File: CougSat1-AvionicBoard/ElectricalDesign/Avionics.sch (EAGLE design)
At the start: 117 parts, among them J3 SWD, J4 CougSat Card, J7 CougSat Card, J8 SWD, J9 SWD, U1 STM32L476RGT, U10 BNO055, U11 128KB, U12 TXS0102DQM, U13 TXS0102DQM, U14 LTC2499, U2 STM32L476RGT, U3 STM32L476RGT, U4 128KB, U5 DRV8837, U6 DRV8837, U7 DRV8837, U8 LTC2499, U9 Venus838FLPx-L, Y1 16MHz ±10ppm, Y2 32.768kHz ±10ppm, Y3 16MHz ±10ppm, Y4 32.768kHz ±10ppm, Y5 16MHz ±10ppm, Y6 32.768kHz ±10ppm, Y7 32.768kHz ±10ppm

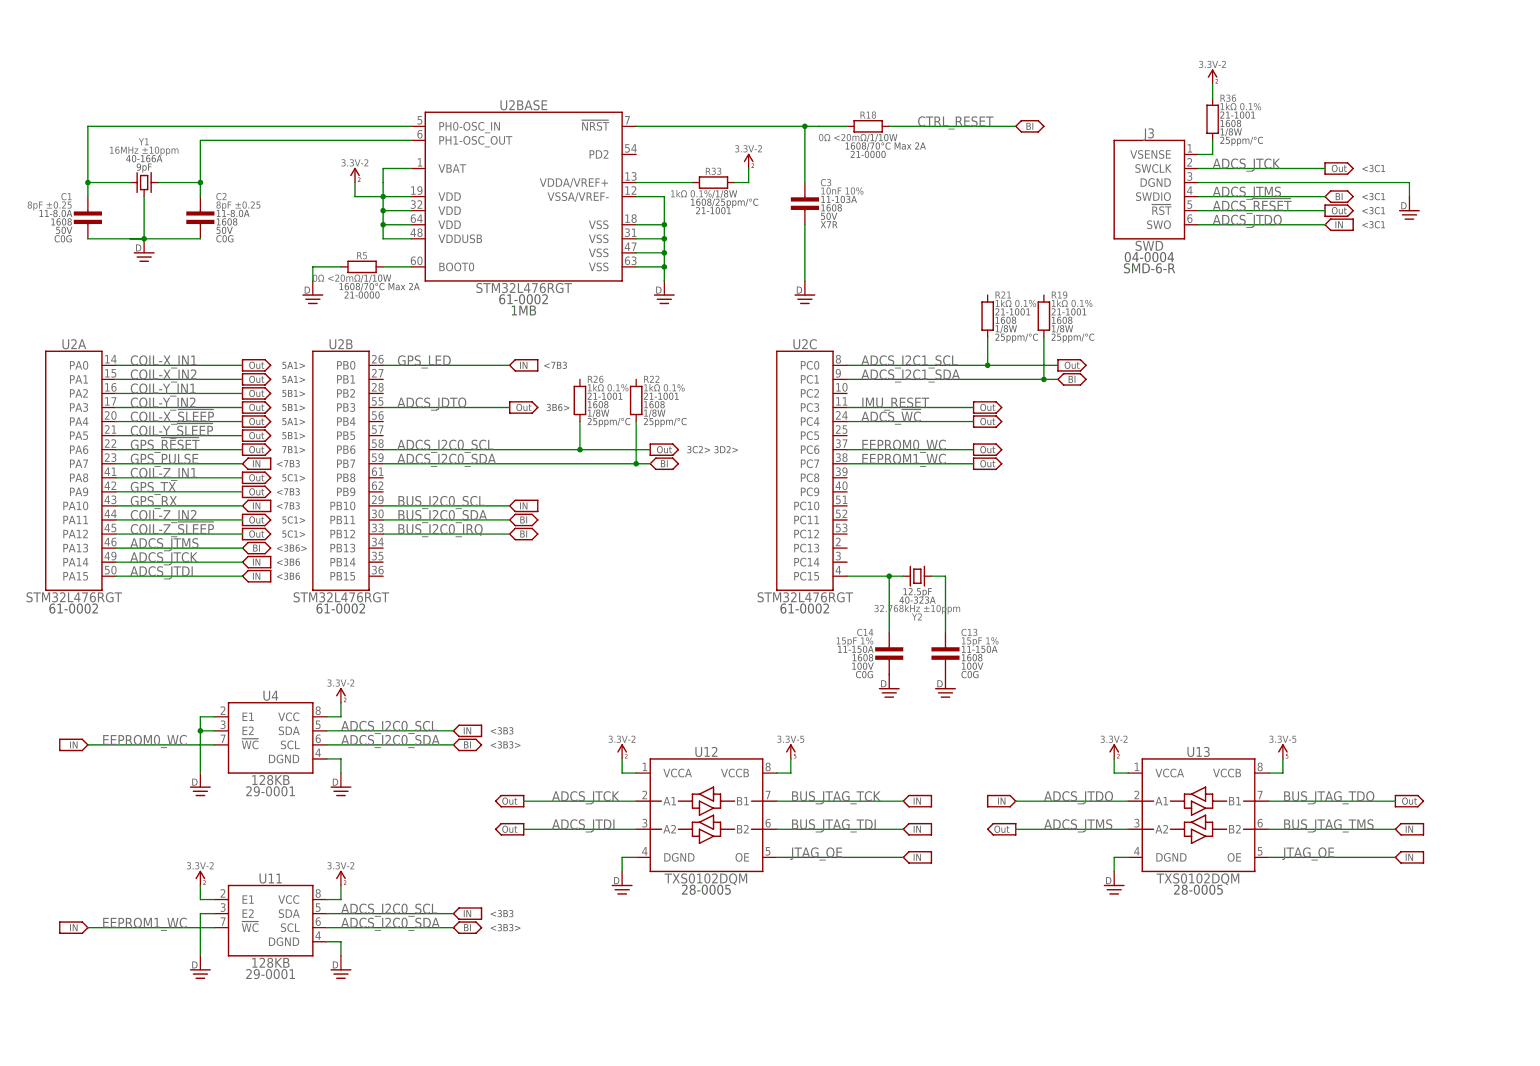
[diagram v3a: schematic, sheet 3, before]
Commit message: Added Final Components to Schematic
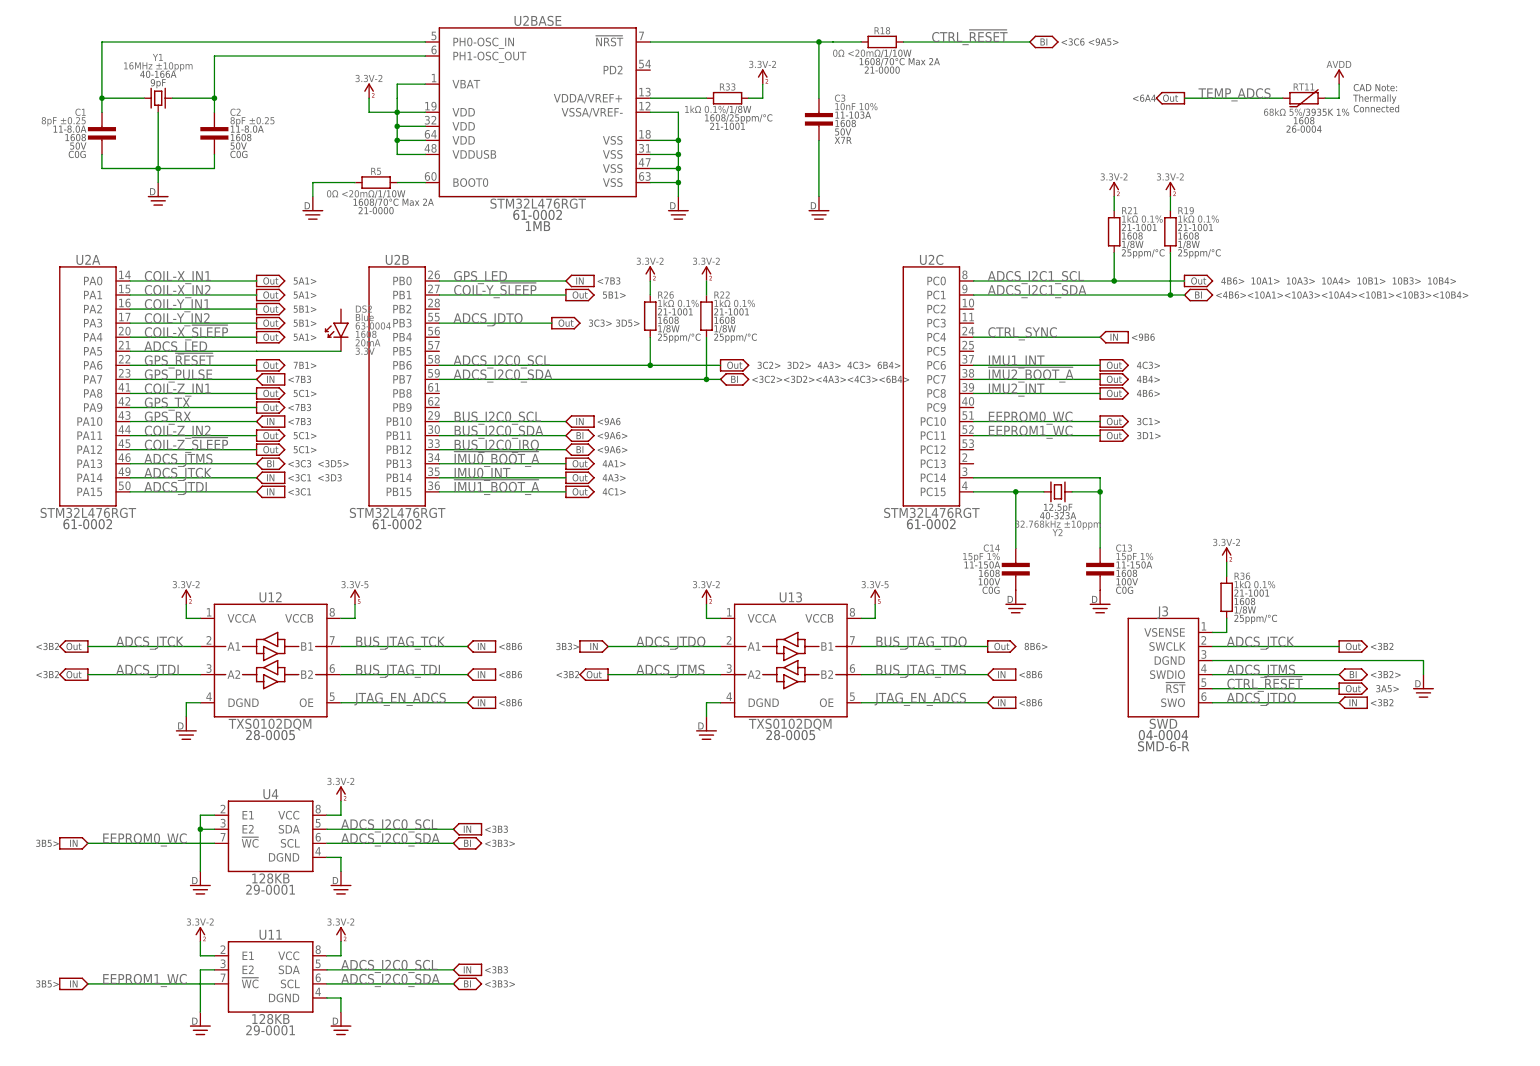
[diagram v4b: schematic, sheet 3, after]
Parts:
- removed L1, L2, L3: xxx Turns, CougsInSpace-Coils:MAGNETORQUER-1UPV-SMD-3030
- added C32, C38: 10nF 10%, CougsInSpace-Capacitors:CAP-H-10NF-1608
- added C33, C39: 100nF 10%, CougsInSpace-Capacitors:CAP-V-100NF-3216
- added C34, C40: 6.8nF 5%, CougsInSpace-Capacitors:CAP-V-6.8NF-1608
- added C35, C41: 100nF 10%, CougsInSpace-Capacitors:CAP-V-100NF-1608
- added C36, C37, C42, C43: 15pF 1%, CougsInSpace-Capacitors:CAP-V-15PF-1608
- added DS2: Blue, CougsInSpace-LEDs:LED-V-BLU-1608
- added R32, R39, R40, R41: 10kΩ 0.1%, CougsInSpace-Resistors:RES-V-10K-1608
- added RT10, RT11, RT12, RT13, RT14, RT8, RT9: 68kΩ 5%, CougsInSpace-Resistors:THERMISTOR-H-68K-1608
- added U15, U16: BNO055, CougsInSpace-Sensors:BNO055
- added Y8, Y9: 32.768kHz ±10ppm, CougsInSpace-Clocks:CRYSTAL-32.768KHZ-SMD3.2X1.5
- J11: value (none) -> -Y
- J12: value (none) -> +Z
- J13: value (none) -> +X
- J14: value (none) -> -Z
- J15: value (none) -> +Y
- J5: value (none) -> -X
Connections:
- net JTAG_OE renamed JTAG_EN_ADCS
- net SPI3_MISO renamed IHU_SPI2_MISO
- net SYS_JTDI renamed IHU_JTDI
- removed net !IMU0_BOOT-A: R25.2, U10.!BOOT_LOAD_PIN
- removed net ADCS_!RESET: J3.!RST
- removed net ADCS_!WC: U2C.PC4
- removed net CTRL_RESET: R18.2, R24.2, R28.2
- removed net I2C_SCL: J11.3, J12.3, J13.3, J14.3, J15.3, J5.3
- removed net I2C_SDA: J11.2, J12.2, J13.2, J14.2, J15.2, J5.2
- removed net IFJR_!RESET: J8.!RST
- removed net IHU_!RESET: J9.!RST
- removed net IMU_RESET: U2C.PC3
- removed net N$11: L2.2, U6.OUT2
- removed net N$14: L3.2, U7.OUT2
- removed net N$31: C20.2, C21.2
- removed net N$33: J16.CD/DAT3
- removed net N$39: C4.1
- removed net N$40: J6.CD/DAT3
- removed net N$41: J2.CMD, J6.CMD
- removed net N$42: U1BASE.VBAT, U1BASE.VDD@1, U1BASE.VDD@2, U1BASE.VDD@3, U1BASE.VDDUSB
- removed net N$43: J2.CLK, J6.CLK
- removed net N$45: J2.DAT0, J6.DAT0
- removed net N$46: J6.SW+
- removed net N$47: J2.CD/DAT3
- removed net N$5: C1.2, C2.2
- removed net N$50: J2.SW+
- removed net N$52: J7POWER.PR_3.3V-3
- removed net N$53: J7POWER.PR_3.3V-4
- removed net N$54: J7POWER.PR_3.3V-5
- removed net N$55: J10.CMD, J16.CMD
- removed net N$56: J10.CLK, J16.CLK
- removed net N$57: J10.DAT0, J16.DAT0
- removed net N$70: J16.SW+
- removed net N$71: J10.CD/DAT3
- removed net N$72: J10.SW+
- removed net N$9: L1.2, U5.OUT2
- removed net SPI1_MISO: J4DATA.BUS_SPI_MISO, U1A.PA6, U3A.PA6
- removed net SPI1_MOSI: J4DATA.BUS_SPI_MOSI, U1A.PA7, U3A.PA7
- removed net SPI1_SCK: J4DATA.BUS_SPI_SCK, U1A.PA5, U3A.PA5
- removed net SPI2_MISO: U3C.PC2
- removed net SPI2_MOSI: U3C.PC3
- removed net SPI2_SCK: U3B.PB10
- removed net SPI3_MOSI: U3C.PC12
- removed net SPI3_SCK: U3C.PC10
- removed net SYS_JTCK-SWCLK: U3A.PA14
- removed net SYS_JTDO-SWO: U3B.PB3
- removed net SYS_JTMS-SWDIO: U3A.PA13
- removed net TEMP_IMU: U8.CH7
- new net !IMU0_BOOT_A: R25.2, U10.!BOOT_LOAD_PIN, U2B.PB13
- new net !IMU1_BOOT_A: R39.2, U15.!BOOT_LOAD_PIN, U2B.PB15
- new net !IMU2_BOOT_A: R41.2, U16.!BOOT_LOAD_PIN, U2C.PC7
- new net ADCS_LED: DS2.C, U2A.PA5
- new net COIL-X_COIL-: J5.4, U5.OUT2
- new net COIL-Y_COIL-: J11.4, U6.OUT2
- new net COIL-Z_+: J12.3
- new net COIL-Z_COIL-: J12.4, U7.OUT2
- new net IFJR_SD_CS0: J16.CD/DAT3, U1A.PA8
- new net IFJR_SD_CS1: J10.CD/DAT3, U1A.PA10
- new net IFJR_SD_SW0: J16.SW+, U1A.PA9
- new net IFJR_SD_SW1: J10.SW+, U1A.PA11
- new net IFJR_SPI0_MISO: J10.DAT0, J16.DAT0, U1A.PA6
- new net IFJR_SPI0_MOSI: J10.CMD, J16.CMD, U1A.PA7
- new net IFJR_SPI0_SCK: J10.CLK, J16.CLK, U1A.PA5
- new net IHU_SD_CS0: J6.CD/DAT3, U3C.PC5
- new net IHU_SD_CS1: J2.CD/DAT3, U3B.PB1
- new net IHU_SD_SW0: J6.SW+, U3B.PB0
- new net IHU_SD_SW1: J2.SW+, U3B.PB2
- new net IHU_SPI0_MISO: J4DATA.BUS_SPI_MISO, U3A.PA6
- new net IHU_SPI0_MOSI: J4DATA.BUS_SPI_MOSI, U3A.PA7
- new net IHU_SPI0_SCK: J4DATA.BUS_SPI_SCK, U3A.PA5
- new net IHU_SPI1_MISO: J4DATA.COM_SPI_MISO, U3C.PC2
- new net IHU_SPI1_MOSI: J4DATA.COM_SPI_MOSI, U3C.PC3
- new net IHU_SPI1_SCK: J4DATA.COM_SPI_SCK, U3B.PB10
- new net IHU_SPI2_MOSI: J2.CMD, J2.DAT0, J6.CMD, J6.DAT0, U3C.PC12
- new net IHU_SPI2_SCK: J2.CLK, J6.CLK, U3C.PC10
- new net IMU1_INT: U15.INT, U2C.PC6
- new net IMU2_INT: U16.INT, U2C.PC8
- new net N$20: C32.2, U15.CAP
- new net N$49: C36.1, U15.XOUT32, Y8.1
- new net N$63: C37.1, U15.XIN32, Y8.2
- new net N$66: C38.2, U16.CAP
- new net N$68: C42.1, U16.XOUT32, Y9.1
- new net N$69: C43.1, U16.XIN32, Y9.2
- new net TEMP_IMU0: RT8.1, U8.CH7
- new net TEMP_IMU1: RT9.1, U8.CH9
- new net TEMP_IMU2: RT10.1, U8.CH10
- net !IMU_RESET: now also R32.1, R40.1, U15.!RESET, U15.COM3, U16.!RESET
- net 3.3V: no longer J11.1, J12.1, J13.1, J14.1, J15.1, J5.1
- net 3.3V_2: now also J13.3, J14.3, R19.2, R21.2, R22.2, R26.2
- net 3.3V_3: now also C33.2, C34.2, C35.2, C39.2, C40.2, C41.2, J7POWER.PR_3.3V-3, R32.2, R39.1, R40.2, R41.1, U15.VDD, U15.VDDIO, U16.VDD, U16.VDDIO
- net 3.3V_4: now also J7POWER.PR_3.3V-4
- net 3.3V_5: now also J7POWER.PR_3.3V-5, U1BASE.VBAT, U1BASE.VDD@1, U1BASE.VDD@2, U1BASE.VDD@3, U1BASE.VDDUSB
- net ADCS_I2C0_SCL: now also U15.COM1
- net ADCS_I2C0_SDA: now also U15.COM0
- net ADCS_I2C1_SCL: now also J11.1, J12.1, J13.1, J14.1, J15.1, J5.1, U16.COM1
- net ADCS_I2C1_SDA: now also J11.2, J12.2, J13.2, J14.2, J15.2, J5.2, U16.COM0
- net AVDD: now also RT10.2, RT11.2, RT12.2, RT13.2, RT14.2, RT8.2, RT9.2
- net COIL-X_COIL+: now also J5.3; no longer L1.1
- net COIL-Y_!SLEEP: now also U2B.PB1; no longer U2A.PA5
- net COIL-Y_COIL+: now also J11.3; no longer L2.1
- net COIL-Z_COIL+: no longer L3.1
- net CTRL_!RESET: now also J3.!RST, J8.!RST, J9.!RST, R18.2, R24.2, R28.2, U3C.PC7
- net CTRL_SYNC: now also U1B.PB0, U2C.PC4, U3C.PC8
- net DGND: now also C1.2, C2.2, C20.2, C21.2, C32.1, C33.1, C34.1, C35.1, C36.2, C37.2, C38.1, C39.1, C4.1, C40.1, C41.1, C42.2, C43.2, U15.COM2, U15.DGND, U15.DGNDIO, U15.PS0, U15.PS1, U16.COM2, U16.COM3, U16.DGND, U16.DGNDIO, U16.PS0, U16.PS1; no longer J11.4, J12.4, J15.4, J5.4
- net EEPROM0_WC: now also U2C.PC10; no longer U2C.PC6
- net EEPROM1_WC: now also U2C.PC11; no longer U2C.PC7
- net IHU_JTCK: now also U3A.PA14
- net IHU_JTDO: now also U3B.PB3
- net IHU_JTMS: now also U3A.PA13
- net IMU0_INT: now also U2B.PB14
- net N$22: now also U2C.PC14
- net TEMP_ADCS: now also RT11.1, U8.CH11; no longer U8.CH9
- net TEMP_H-BRIDGE-X: now also U8.CH13; no longer U8.CH10
- net TEMP_H-BRIDGE-Y: now also U8.CH14; no longer U8.CH11
- net TEMP_H-BRIDGE-Z: now also U8.CH15; no longer U8.CH12
- net TEMP_IHU: now also RT14.1
- net TEMP_SD_IHU0: now also RT12.1
- net TEMP_SD_IHU1: now also RT13.1
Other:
- note added: "10A1>"
- note added: "10A3>"
- note added: "10A4>"
- note added: "3A5>"
- note added: "3B5>"
- note added: "3C1>"
- note added: "3C2> 3D2> 4A3> 4C3> 6B4>"
- note added: "3C3> 3D5>"
- note added: "3D1>"
- note added: "4A1>"
- note added: "4A3>"
- note added: "4B4>"
- note added: "4B6>"
- note added: "4B6> 10A1> 10A3> 10A4> 10B1> 10B3> 10B4>"
- note added: "4C1>"
- note added: "4C3>"
- note added: "5A2>"
- note added: "5A3>"
- note added: "5B2>"
- note added: "5B3>"
- note added: "5C2>"
- note added: "5C3>"
- note added: "6A1>"
- note added: "7C3>"
- note added: "8A2>"
- note added: "8A5>"
- note added: "8B2>"
- note added: "8B6>"
- note added: "8C2>"
- note added: "8C3>"
- note added: "8C6>"
- note added: "8D2>"
- note added: "8D3>"
- note added: "9A1>"
- note added: "9B2>"
- note added: "9B3>"
- note added: "9B4>"
- note added: "9B5>"
- note added: "9B6>"
- note added: "9C2>"
- note added: "9C4>"
- note added: "9D2>"
- note added: "9D4>"
- note added: "9D6>"
- note added: "<10A1"
- note added: "<10A3"
- note added: "<10A4"
- note added: "<3A5"
- note added: "<3B2>"
- note added: "<3B5"
- note added: "<3B5>"
- note added: "<3C1 <3D3"
- note added: "<3C2><3D2><4A3><4C3><6B4>"
- note added: "<3C3 <3D5>"
- note added: "<3C6 <9A5>"
- note added: "<4A1"
- note added: "<4B6><10A1><10A3><10A4><10B1><10B3><10B4>"
- note added: "<5A3"
- note added: "<5A4"
- note added: "<5B3"
- note added: "<5B4"
- note added: "<5C3"
- note added: "<5C4"
- note added: "<6A2"
- note added: "<6A4"
- note added: "<6C2"
- note added: "<8B2"
- note added: "<8B2>"
- note added: "<8B3"
- note added: "<8B4"
- note added: "<8B6"
- note added: "<8B6>"
- note added: "<8C2"
- note added: "<8C2>"
- note added: "<8C6"
- note added: "<8C6 <9A5>"
- note added: "<8C6>"
- note added: "<8D2"
- note added: "<9A6"
- note added: "<9A6>"
- note added: "<9B2"
- note added: "<9B2>"
- note added: "<9B3"
- note added: "<9B3 <3B3"
- note added: "<9B3>"
- note added: "<9B3><3B3>"
- note added: "<9B4"
- note added: "<9B4 3B5> 8B3>"
- note added: "<9B4><3A5><8A5><9A5>"
- note added: "<9B6"
- note added: "<9B6>"
- note added: "<9C2"
- note added: "<9C6"
- note added: "<9C6>"
- note added: "<9D2"
- note added: "<9D6 <9B6>"
- note added: "<9D6>"
- note added: "\ <3B3"
- note removed: "3B6>"
- note removed: "3C2> 3D2>"
- moved on the sheet: C1, C11, C12, C13, C14, C17, C18, C2, C23, C25, C26, C3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

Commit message: Update Avionics.sch
Adjusted schematic
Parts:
- removed C20, C21: 8pF ±0.25, CougsInSpace-Capacitors:CAP-V-8PF-1608
- removed J7: CougSat Card, CougsInSpace-Boards:CIS_CARD-OPEN+X
- removed Y5: 16MHz ±10ppm, CougsInSpace-Clocks:CRYSTAL-16MHZ-SMD3.2X1.5
- added C44, C46, C47, C48, C49, C54, C55, C56, C57, C60, C61, C62, C63: 100nF 10%, CougsInSpace-Capacitors:CAP-V-100NF-1608
- added C45: 100nF 10%, CougsInSpace-Capacitors:CAP-V-100NF-3216
- added C58, C59: 8pF ±0.25, CougsInSpace-Capacitors:CAP-V-8PF-1608
- added DS3: Yellow, CougsInSpace-LEDs:LED-H-YLW-1608
- added DS5: Green, CougsInSpace-LEDs:LED-H-GRN-1608
- added R42, R46: 1kΩ 0.1%, CougsInSpace-Resistors:RES-H-1K-1608
- added R43, R44: 10kΩ 0.1%, CougsInSpace-Resistors:RES-V-10K-1608
- added R45: 0Ω <20mΩ, CougsInSpace-Resistors:RES-H-0-1608
- added U17, U18: TXS0102DQM, CougsInSpace-IC-Logic:LEVEL_SHIFTER-2BIT-XSON-8
- added Y10: 16MHz ±10ppm, CougsInSpace-Clocks:CRYSTAL-16MHZ-SMD-4025
- C34: value 6.8nF 5% -> 100nF 10%; device CougsInSpace-Capacitors:CAP-V-6.8NF-1608 -> CougsInSpace-Capacitors:CAP-V-100NF-1608
- C35, C41, C8: value 100nF 10% -> 6.8nF 5%; device CougsInSpace-Capacitors:CAP-V-100NF-1608 -> CougsInSpace-Capacitors:CAP-V-6.8NF-1608
- C40, C6: value 6.8nF 5% -> 100nF 10%; device CougsInSpace-Capacitors:CAP-V-6.8NF-1608 -> CougsInSpace-Capacitors:CAP-V-100NF-3216
- DS2: device CougsInSpace-LEDs:LED-V-BLU-1608 -> CougsInSpace-LEDs:LED-H-BLU-1608
- R13: value 560Ω 1% -> 1kΩ 0.1%; device CougsInSpace-Resistors:RES-H-560R-1608 -> CougsInSpace-Resistors:RES-H-1K-1608
- R27: value 0Ω <20mΩ -> 1kΩ 0.1%; device CougsInSpace-Resistors:RES-H-0-1608 -> CougsInSpace-Resistors:RES-H-1K-1608
- Y1, Y3: device CougsInSpace-Clocks:CRYSTAL-16MHZ-SMD3.2X1.5 -> CougsInSpace-Clocks:CRYSTAL-16MHZ-SMD-4025
- Y2, Y4, Y6, Y7, Y8, Y9: device CougsInSpace-Clocks:CRYSTAL-32.768KHZ-SMD3.2X1.5 -> CougsInSpace-Clocks:CRYSTAL-32.768KHZ-SMD-3215
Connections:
- removed net 3.3V: C29.1, C7.1, U14.VCC, U8.VCC
- removed net ADCS_LED: DS2.C, U2A.PA5
- removed net COIL-X_SLEEP: U5.!SLEEP
- removed net COIL-Y_SLEEP: U6.!SLEEP
- removed net COIL-Z_SLEEP: U7.!SLEEP
- removed net IHU_GPIO-6: J4GPIO.GPIO-6, U3A.PA9
- removed net IHU_GPIO-7: J4GPIO.GPIO-7, U3A.PA10
- removed net IHU_GPIO-8: J4GPIO.GPIO-8, U3A.PA11
- removed net IHU_GPIO-9: J4GPIO.GPIO-9, U3A.PA12
- removed net N$32: R27.2, U3BASE.BOOT0
- removed net N$34: C20.1, U3BASE.PH0-OSC_IN, Y5.1
- new net IFJR_LED: DS5.A, U1A.PA4
- new net IHU_LED: DS2.A, DS3.A, U2A.PA5, U3A.PA9
- new net JTAG_EN_IHU: J4JTAG.BUS_JTAG_EN-1, U17.OE, U18.OE, U1C.PC4
- new net N$14: C58.1, U3BASE.PH0-OSC_IN, Y10.1
- new net N$15: C59.1, U3BASE.PH1-OSC_OUT, Y10.2
- new net N$21: R45.2, U3BASE.BOOT0
- new net N$31: DS5.C, R46.1
- new net N$5: DS2.C, R42.1
- net !IMU0_BOOT_A: now also R43.1; no longer R25.2
- net !IMU1_BOOT_A: now also R39.1; no longer R39.2
- net 3.3V_0: now also C60.1, C61.1, C62.1, C63.1, J4POWER.PR_3.3V-0, U14.CA0, U14.VCC; no longer J7POWER.PR_3.3V-0
- net 3.3V_1: now also J4POWER.PR_3.3V-1; no longer J7POWER.PR_3.3V-1
- net 3.3V_2: now also C46.1, C47.1, C48.1, C49.1, J4POWER.PR_3.3V-2, U17.VCCA, U18.VCCA, U8.VCC; no longer J7POWER.PR_3.3V-2
- net 3.3V_3: now also C33.1, C35.1, C39.1, C40.1, C41.1, C45.1, C5.1, C6.1, C8.1, R39.2, R43.2; no longer C33.2, C34.2, C35.2, C39.2, C40.2, C41.2, C5.2, C6.2, C8.2, J7POWER.PR_3.3V-3, R25.1, R39.1
- net 3.3V_4: now also J4POWER.PR_3.3V-4; no longer J7POWER.PR_3.3V-4
- net 3.3V_5: now also C54.1, C55.1, C56.1, C57.1, J4POWER.PR_3.3V-5, R25.2, R44.2, U17.VCCB, U18.VCCB; no longer J7POWER.PR_3.3V-5
- net 3.3V_6: now also C29.1, C34.1, C44.1, C7.1
- net BUS_JTAG_TCK: now also U17.B1
- net BUS_JTAG_TDI: now also U17.B2
- net BUS_JTAG_TDO: now also U18.B1
- net BUS_JTAG_TMS: now also U18.B2
- net CHASSIS: now also J4POWER.CHASSIS; no longer J7POWER.CHASSIS
- net COIL-X_!SLEEP: now also U5.!SLEEP
- net COIL-Y_!SLEEP: now also U6.!SLEEP
- net COIL-Z_!SLEEP: now also U7.!SLEEP
- net DGND: now also C33.2, C34.2, C35.2, C39.2, C40.2, C41.2, C44.2, C45.2, C46.2, C47.2, C48.2, C49.2, C5.2, C54.2, C55.2, C56.2, C57.2, C58.2, C59.2, C6.2, C60.2, C61.2, C62.2, C63.2, C8.2, R27.2, R42.2, R45.1, R46.2, U17.DGND, U18.DGND, Y10.GND; no longer C20.2, C21.2, C33.1, C34.1, C35.1, C39.1, C40.1, C41.1, C5.1, C6.1, C8.1, R27.1, U14.CA0, Y5.GND
- net IHU_JTCK: now also U17.A1
- net IHU_JTDI: now also U17.A2
- net IHU_JTDO: now also U18.A1
- net IHU_JTMS: now also U18.A2
- net IHU_SD_CS0: now also R25.1
- net IHU_SD_CS1: now also R44.1
- net N$7: now also DS3.C, R27.1; no longer C21.1, U3BASE.PH1-OSC_OUT, Y5.2
- net PGND: now also J4POWER.PGND; no longer J7POWER.PGND
- net VBATT_5: now also J4POWER.PR_BATT-5; no longer J7POWER.PR_BATT-5
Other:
- note added: "10B4>"
- note added: "10C4>"
- note added: "3A6>"
- note added: "3D3>"
- note added: "3D5>"
- note added: "5A4>"
- note added: "5A5>"
- note added: "5B4>"
- note added: "5B5>"
- note added: "5C4>"
- note added: "5C5>"
- note added: "8A6>"
- note added: "9A5>"
- note added: "9A6>"
- note added: "9B6> 3B5> 8B3>"
- note added: "9D1>"
- note added: "9D6> 9D1>"
- note added: "<10B4"
- note added: "<10C4"
- note added: "<3C6 <9B6>"
- note added: "<5A5"
- note added: "<5B2"
- note added: "<5B5"
- note added: "<5C2"
- note added: "<5C5"
- note added: "<5D2"
- note added: "<8C6 <9B6>"
- note added: "<9B4><3A6><8A6><9A6>"
- note added: "<9C1"
- note added: "<9C6 <9C1"
- note added: "<9D6><9D1"
- note added: "CAD Note: Thermally Connected to µController"
- note added: "Page 10: Power & ADCS Jacks"
- note added: "Page 1: Block Diagram Page 2: Power Rails Page 3: ADCS Page 4: IMUs Page 5: H-Bridges Page 6: ADCs Page 7: GPS Page 8: IFJR Page 9: C&DH"
- note removed: "3A5>"
- note removed: "5A1>"
- note removed: "5A3>"
- note removed: "5B1>"
- note removed: "5B3>"
- note removed: "5C1>"
- note removed: "5C3>"
- note removed: "8A2>"
- note removed: "9A1>"
- note removed: "9B5>"
- note removed: "9C2>"
- note removed: "9D2>"
- note removed: "9D6>"
- note removed: "<3C6 <9A5>"
- note removed: "<5A3"
- note removed: "<5A4"
- note removed: "<5B3"
- note removed: "<5B4"
- note removed: "<5C3"
- note removed: "<5C4"
- note removed: "<8C6 <9A5>"
- note removed: "<9B4 3B5> 8B3>"
- note removed: "<9B4><3A5><8A5><9A5>"
- note removed: "<9C6"
- note removed: "<9D2"
- note removed: "<9D6>"
- note removed: "PR_3.3V-3"
- note removed: "Page 1: Block Diagram Page 2: Power Rails"
